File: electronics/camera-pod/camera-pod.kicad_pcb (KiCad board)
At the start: 2 copper layers, 40 x 27 mm, 16 parts, among them J1 LEAD, J2 MEGA, U1 AMS1117-3.3

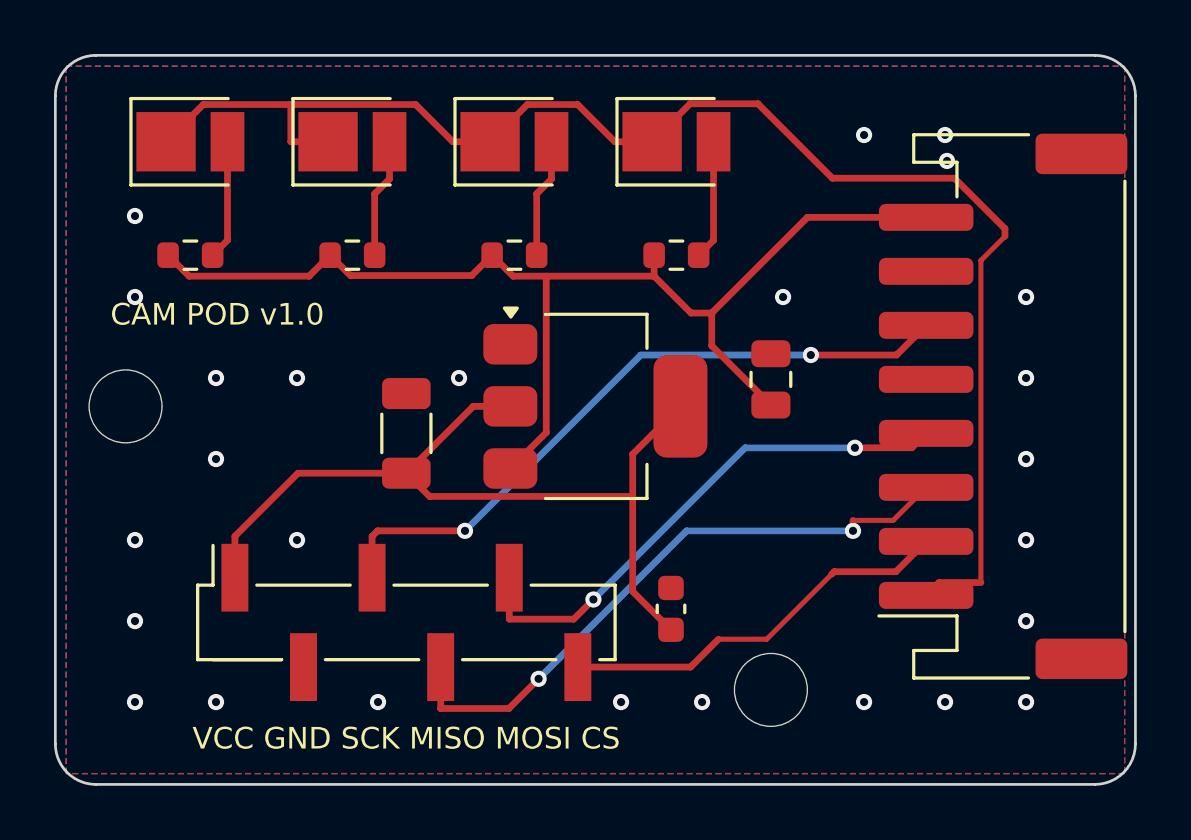
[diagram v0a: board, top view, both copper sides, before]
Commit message: Camera pod: the PCBA review's fixes
P1: the LED resistors are 100 Ohm 0805 (C17408, a basic part; no 82 Ohm
exists as a basic 0805 or 1206).  Over the LEDs' Vf spread at that
current (about 2.65-3.2 V) and CAM_5V at 5.0-5.2 V that gives 18-26 mA
per LED, at most 66 mW in a 125 mW resistor and 102 mA for the four,
inside the node's camera budget.  56 Ohm 0603 gave 36-44 mA and up to
108 mW in 100 mW.  The light drops by about a third from the 32 mA
first planned, about 0.6 EV, which the Mega's auto-exposure takes.
P2: the AMS1117's ringing on its 22 uF MLCC is on the bring-up list,
with the LED current.  P3: a CAM_5V load switch on IO5/IO6 noted for a
later node.

The CPL audit agrees on all 14 parts.  ERC 0, DRC 0, parity 0, 0
unconnected; the BOM follows.

Co-Authored-By: Claude Opus 5.5 <noreply@anthropic.com>
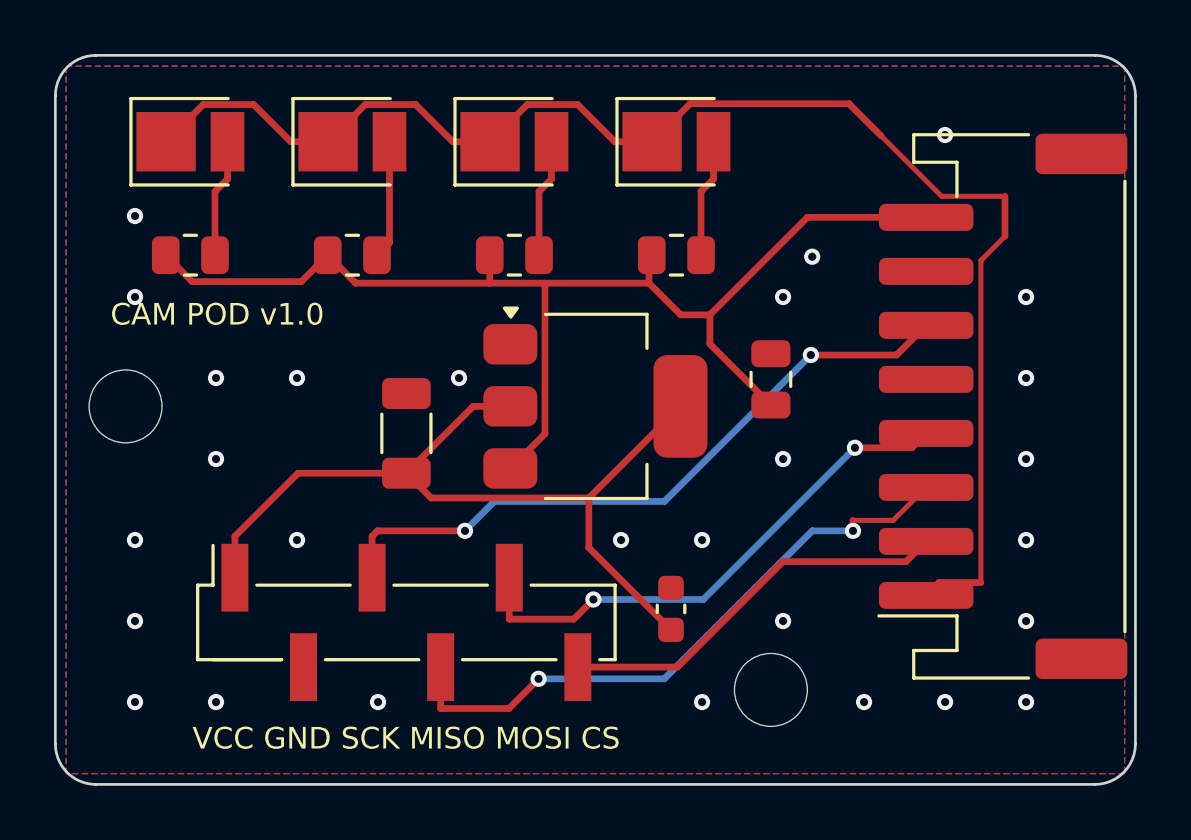
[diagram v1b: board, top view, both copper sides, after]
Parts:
- R1, R2, R3, R4: value 56 -> 100; footprint Resistor_SMD:R_0603_1608Metric -> Resistor_SMD:R_0805_2012Metric
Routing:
- net /Pod/LED_K: track 54.3 -> 53.4 mm
- net /Pod/CAM_5V: track 44.5 -> 45.2 mm
- net GND: vias 26 -> 28

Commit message: Power pads connect solid on the DATA ×4, the DATA port and the camera pod
The rule from d58f976, applied to the three boards. Each one declares its power nets in design.py:
- DATA ×4: GND, +5V, each port's 5V_SW and VBUS
- DATA port: GND, VBUS
- camera pod: GND, CAM_5V
pcbgen then connects their IC and connector pins solid to the pours. A small part with an end on a
track keeps its reliefs. The .kicad_dru carries both rules.

Now solid:
- DATA ×4: the four receptacles' and J1's GND pins; the hub's, expanders', INA226s', switches' and
  ESDs' GND pins and exposed pads; the LDO's VIN, EN and GND on its islands. Eighteen GND pads the
  pour didn't reach (USB4105 A1/A12/B1/B12 among them) now take it directly, and their tie tracks go
  (25 segments, 11 vias). The ports' 5V_SW and VBUS run in tracks, so their pads don't change.
- DATA port: J1's four GND pins, J2's two, the ESD's GND.
- Camera pod: J1's two GND pins, J2's GND, the AMS1117's GND.

Worst relieved power-net pad, before → after:
- DATA ×4: INA226 GND (U102.7) on 1 spoke, 0.29 mm → solid. Now the worst is a GND decoupling cap or
  pull-down (C201.2, R201.2...) on 1 spoke of 0.40 mm, a signal-level current.
- DATA port: J1's GND pins and U1.2 on 1 spoke, 0.40 mm → solid. Now the worst is C1 / C2 / the shell
  tabs on 3 spokes, 1.20 mm.
- Camera pod: U1.1, J1.5 / J1.7, C1, C3 on 3 spokes, 1.20 mm. Now U1.1 and J1's GND are solid; the
  worst is C1 / C3 on 3 spokes, 1.20 mm.

Same routes re-imported: only GND ties and stitching vias move. ERC/DRC 0, parity 0, 0 unconnected on
all three. CPL and BOM unchanged, so the CPL audit stands. Renders, PDFs and gerbers regenerated.

Co-Authored-By: Claude Opus 5.5 <noreply@anthropic.com>
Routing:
- net GND: vias 28 -> 32

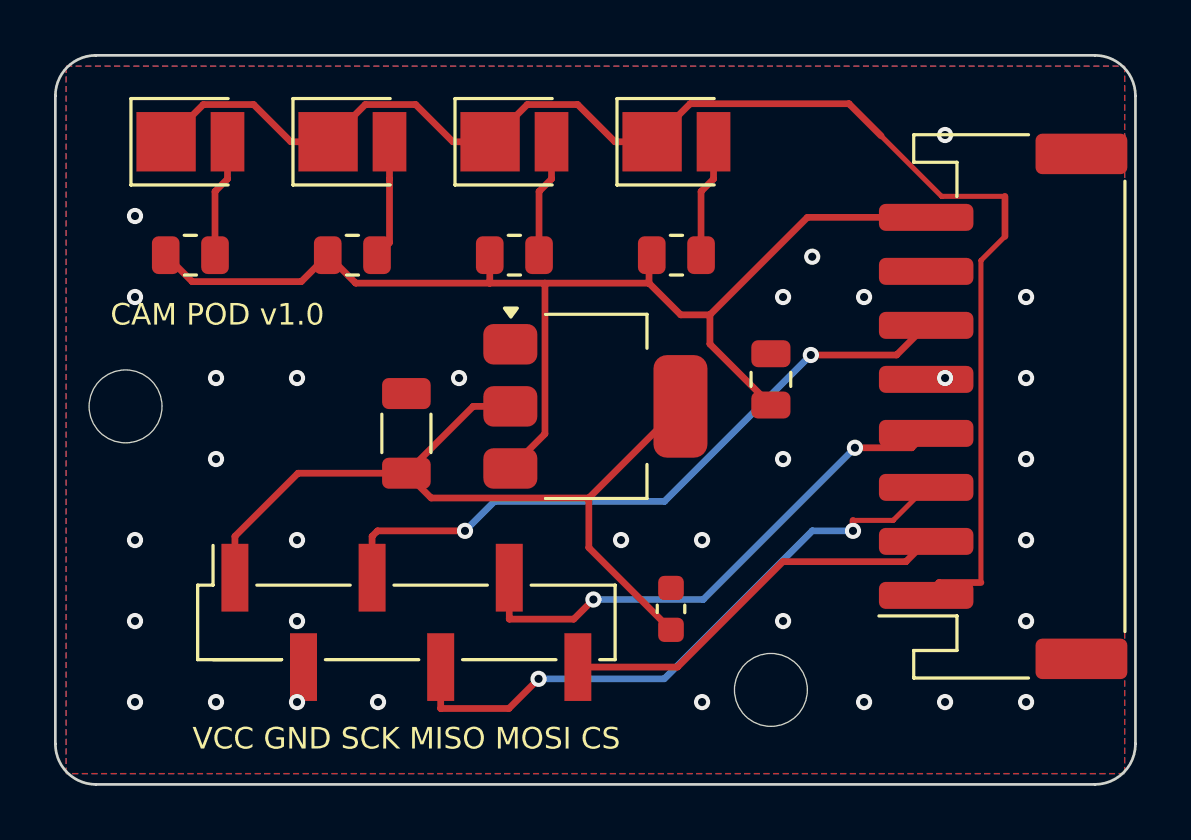
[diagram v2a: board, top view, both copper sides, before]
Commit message: Boards: tracks straightened after routing, bends ranked; bay node and hub re-routed
Freerouting leaves staircases of 45° and straight segments where one bend
would do: they are no longer than the straight route, so nothing preferred it.

- pcbgen.tidy_tracks now runs on every board after the import: a run of up
  to 12 router segments becomes the fewest straight and 45° segments joining
  its ends (octilinear.py: one, one bend, or a dogleg on one of the run's own
  lines), at no more length and with every clearance kept.  Differential
  pairs, drawn tracks, exclusive cores, fan-out reservations and footprint
  keep-outs are left alone.  tools/kicad.sh <board> --tidy runs it on a
  routed board without re-routing.
- route_metrics counts bends; route_farm ranks them at 0.5 mm each.
- Bay node: In2's +5V outline stops at x 21.7, off the +3V3 one.  Re-routed
  by the portfolio (noneck): 504 bends, 435 vias, 2183 mm (was 631, 401, 2270).
- Power hub: buck-vin is exclusive (14 of 17 runs clean, 2 before).
  Re-routed (planevia50): 655 bends, 436 vias, 3447 mm (was 767, 433, 3537).
- DATA x4 v2: the drawn switch feeds stay (no clean run without them); its
  routing straightened in place, the tidy settings now the default.
- Camera pod straightened in place (59 -> 48 bends); data port unchanged.

ERC, copper DRC and parity clean on all five; fab outputs, the DATA x4 v2
panel and the viewer's models regenerated.

Co-Authored-By: Claude Opus 5.5 <noreply@anthropic.com>
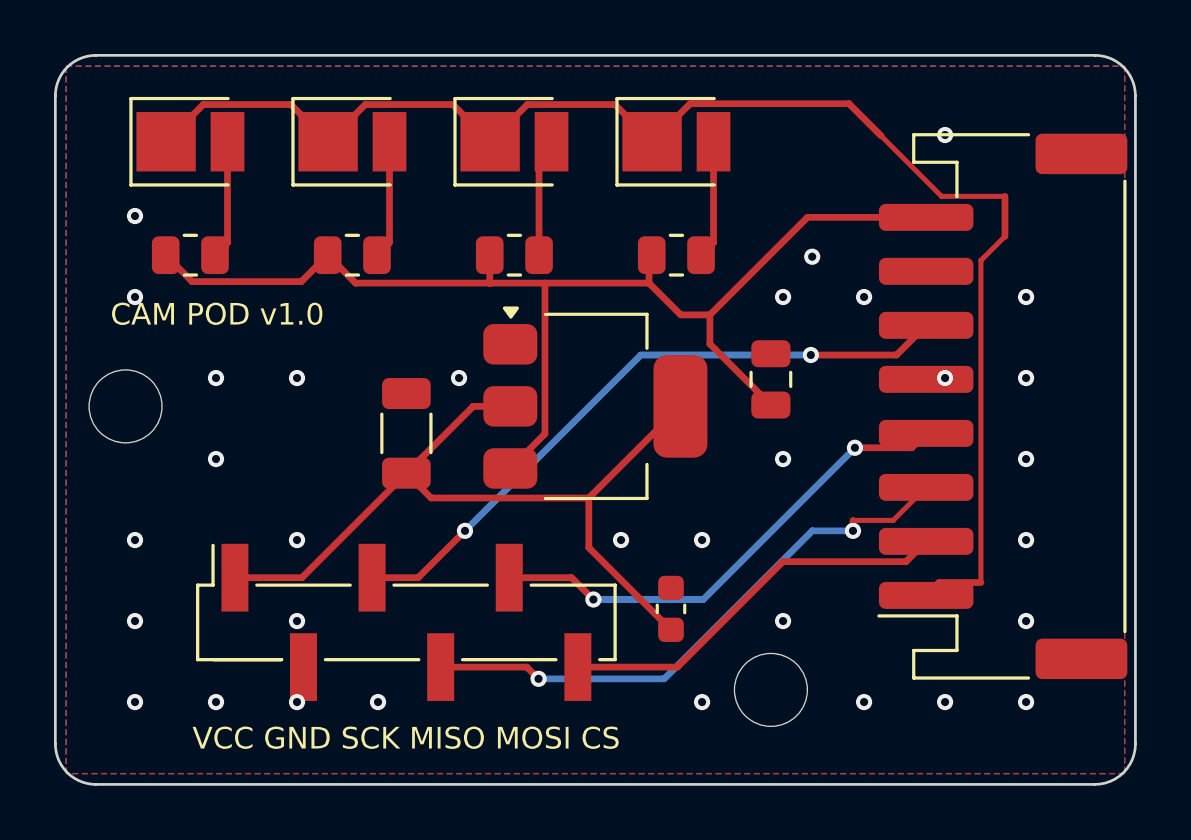
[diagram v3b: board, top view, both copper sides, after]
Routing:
- net /Pod/MISO: track 23.1 -> 21.3 mm
- net /Pod/MOSI: track 19.8 -> 18.3 mm
- net /Pod/SCK: track 25.3 -> 24.4 mm
- net +3V3: track 31.8 -> 30.9 mm
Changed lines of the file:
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@@
-	)
-	(segment
-		(start 13 15.475)
-		(end 8.9863 15.475)
-		(width 0.25)
-		(layer "F.Cu")
-		(net "+3V3")
 	)
 	(segment
@@
 	)
 	(segment
+		(start 13 15.475)
+		(end 9.13 19.345)
+		(width 0.25)
+		(layer "F.Cu")
+		(net "+3V3")
+	)
+	(segment
 		(start 15.475 13)
 		(end 16.85 13)
@@
 	)
 	(segment
-		(start 8.9863 15.475)
-		(end 6.65 17.8113)
-		(width 0.25)
-		(layer "F.Cu")
-		(net "+3V3")
-	)
-	(segment
-		(start 6.65 19.345)
-		(end 6.65 17.8113)
+		(start 9.13 19.345)
+		(end 6.65 19.345)
 		(width 0.25)
 		(layer "F.Cu")
@@
 	)
 	(segment
-		(start 11.9313 17.61)
-		(end 11.73 17.8113)
+		(start 13.4355 19.345)
+		(end 11.73 19.345)
 		(width 0.25)
 		(layer "F.Cu")
@@
 	(segment
 		(start 15.1705 17.61)
-		(end 11.9313 17.61)
+		(end 13.4355 19.345)
 		(width 0.25)
 		(layer "F.Cu")
 		(net "/Pod/SCK")
 	)
-	(segment
-		(start 11.73 19.345)
-		(end 11.73 17.8113)
-		(width 0.25)
-		(layer "F.Cu")
+	(via
+		(at 27.9793 11.0976)
+		(size 0.6)
+		(drill 0.3)
+		(layers "F.Cu" "B.Cu")
 		(net "/Pod/SCK")
 	)
 	(via
-		(at 27.9793 11.0976)
+		(at 15.1705 17.61)
 		(size 0.6)
 		(drill 0.3)
@@
 		(net "/Pod/SCK")
 	)
-	(via
-		(at 15.1705 17.61)
-		(size 0.6)
-		(drill 0.3)
-		(layers "F.Cu" "B.Cu")
-		(net "/Pod/SCK")
-	)
-	(segment
-		(start 22.5581 16.5188)
-		(end 16.2617 16.5188)
+	(segment
+		(start 21.6829 11.0976)
+		(end 15.1705 17.61)
 		(width 0.25)
 		(layer "B.Cu")
@@
 	(segment
 		(start 27.9793 11.0976)
-		(end 22.5581 16.5188)
+		(end 21.6829 11.0976)
 		(width 0.25)
 		(layer "B.Cu")
 		(net "/Pod/SCK")
-	)
-	(segment
-		(start 16.2617 16.5188)
-		(end 15.1705 17.61)
-		(width 0.25)
-		(layer "B.Cu")
-		(net "/Pod/SCK")
-	)
-	(segment
-		(start 17.8955 23.09)
-		(end 16.7968 24.1887)
-		(width 0.25)
-		(layer "F.Cu")
-		(net "/Pod/MISO")
 	)
 	(segment
@@
 	)
 	(segment
+		(start 17.8955 23.09)
+		(end 17.4605 22.655)
+		(width 0.25)
+		(layer "F.Cu")
+		(net "/Pod/MISO")
+	)
+	(segment
+		(start 17.4605 22.655)
+		(end 14.27 22.655)
+		(width 0.25)
+		(layer "F.Cu")
+		(net "/Pod/MISO")
+	)
+	(segment
 		(start 29.5398 17.61)
 		(end 29.5398 17.2218)
@@
 		(net "/Pod/MISO")
 	)
-	(segment
-		(start 14.27 22.655)
-		(end 14.27 24.1887)
-		(width 0.25)
-		(layer "F.Cu")
-		(net "/Pod/MISO")
-	)
-	(segment
-		(start 16.7968 24.1887)
-		(end 14.27 24.1887)
-		(width 0.25)
-		(layer "F.Cu")
-		(net "/Pod/MISO")
-	)
 	(via
 		(at 29.5398 17.61)
@@
 	)
 	(segment
-		(start 19.9264 20.152)
-		(end 19.1997 20.8787)
+		(start 19.1194 19.345)
+		(end 16.81 19.345)
 		(width 0.25)
 		(layer "F.Cu")
@@
 	)
 	(segment
+		(start 19.9264 20.152)
+		(end 19.1194 19.345)
+		(width 0.25)
+		(layer "F.Cu")
+		(net "/Pod/MOSI")
+	)
+	(segment
 		(start 31.7167 14.5333)
 		(end 32.25 14)
@@
 		(net "/Pod/MOSI")
 	)
-	(segment
-		(start 19.1997 20.8787)
-		(end 16.81 20.8787)
-		(width 0.25)
-		(layer "F.Cu")
-		(net "/Pod/MOSI")
-	)
-	(segment
-		(start 16.81 19.345)
-		(end 16.81 20.8787)
-		(width 0.25)
-		(layer "F.Cu")
-		(net "/Pod/MOSI")
-	)
 	(via
 		(at 29.6116 14.5333)
@@
 	)
 	(segment
-		(start 5.9125 5.0412)
-		(end 5.9125 7.4)
+		(start 5.9125 7.4)
+		(end 6.375 6.9375)
 		(width 0.25)
 		(layer "F.Cu")
@@
 	)
 	(segment
-		(start 6.375 3.2)
-		(end 6.375 4.5787)
+		(start 6.375 6.9375)
+		(end 6.375 3.2)
 		(width 0.25)
 		(layer "F.Cu")
 		(net "/Pod/LED_A1")
-	)
-	(segment
-		(start 6.375 4.5787)
-		(end 5.9125 5.0412)
-		(width 0.25)
-		(layer "F.Cu")
-		(net "/Pod/LED_A1")
-	)
-	(segment
-		(start 10.1 3.2)
-		(end 11.4787 1.8213)
-		(width 0.25)
-		(layer "F.Cu")
-		(net "/Pod/LED_K")
 	)
 	(segment
@@
 	)
 	(segment
-		(start 19.3426 1.8213)
-		(end 20.7213 3.2)
+		(start 11.4787 1.8213)
+		(end 14.7213 1.8213)
 		(width 0.25)
 		(layer "F.Cu")
@@
 		(start 16.1 3.2)
 		(end 17.4787 1.8213)
+		(width 0.25)
+		(layer "F.Cu")
+		(net "/Pod/LED_K")
+	)
+	(segment
+		(start 8.7213 1.8213)
+		(end 5.4787 1.8213)
 		(width 0.25)
 		(layer "F.Cu")
@@
 	)
 	(segment
-		(start 13.3426 1.8213)
-		(end 14.7213 3.2)
+		(start 35.1678 6.7055)
+		(end 35.1678 5.2218)
+		(width 0.25)
+		(layer "F.Cu")
+		(net "/Pod/LED_K")
+	)
+	(segment
+		(start 32.7257 19.5243)
+		(end 34.2781 19.5243)
+		(width 0.25)
+		(layer "F.Cu")
+		(net "/Pod/LED_K")
+	)
+	(segment
+		(start 10.1 3.2)
+		(end 11.4787 1.8213)
+		(width 0.25)
+		(layer "F.Cu")
+		(net "/Pod/LED_K")
+	)
+	(segment
+		(start 14.7213 1.8213)
+		(end 16.1 3.2)
+		(width 0.25)
+		(layer "F.Cu")
+		(net "/Pod/LED_K")
+	)
+	(segment
+		(start 29.3919 1.7918)
+		(end 23.5082 1.7918)
+		(width 0.25)
+		(layer "F.Cu")
+		(net "/Pod/LED_K")
+	)
+	(segment
+		(start 20.7213 1.8213)
+		(end 22.1 3.2)
+		(width 0.25)
+		(layer "F.Cu")
+		(net "/Pod/LED_K")
+	)
+	(segment
+		(start 32.25 20)
+		(end 32.7257 19.5243)
 		(width 0.25)
 		(layer "F.Cu")
@@
 	)
 	(segment
-		(start 35.1678 6.7055)
-		(end 35.1678 5.2218)
-		(width 0.25)
-		(layer "F.Cu")
-		(net "/Pod/LED_K")
-	)
-	(segment
-		(start 32.7257 19.5243)
-		(end 34.2781 19.5243)
-		(width 0.25)
-		(layer "F.Cu")
-		(net "/Pod/LED_K")
-	)
-	(segment
-		(start 8.7213 3.2)
-		(end 7.3426 1.8213)
-		(width 0.25)
-		(layer "F.Cu")
-		(net "/Pod/LED_K")
-	)
-	(segment
-		(start 29.3919 1.7918)
-		(end 23.5082 1.7918)
-		(width 0.25)
-		(layer "F.Cu")
-		(net "/Pod/LED_K")
-	)
-	(segment
-		(start 16.1 3.2)
-		(end 14.7213 3.2)
-		(width 0.25)
-		(layer "F.Cu")
-		(net "/Pod/LED_K")
-	)
-	(segment
-		(start 7.3426 1.8213)
-		(end 5.4787 1.8213)
-		(width 0.25)
-		(layer "F.Cu")
-		(net "/Pod/LED_K")
-	)
-	(segment
-		(start 32.25 20)
-		(end 32.7257 19.5243)
-		(width 0.25)
-		(layer "F.Cu")
-		(net "/Pod/LED_K")
-	)
-	(segment
-		(start 10.1 3.2)
-		(end 8.7213 3.2)
-		(width 0.25)
-		(layer "F.Cu")
-		(net "/Pod/LED_K")
-	)
-	(segment
-		(start 17.4787 1.8213)
-		(end 19.3426 1.8213)
-		(width 0.25)
-		(layer "F.Cu")
-		(net "/Pod/LED_K")
-	)
-	(segment
-		(start 11.4787 1.8213)
-		(end 13.3426 1.8213)
-		(width 0.25)
-		(layer "F.Cu")
-		(net "/Pod/LED_K")
-	)
-	(segment
-		(start 22.1 3.2)
-		(end 20.7213 3.2)
-		(width 0.25)
-		(layer "F.Cu")
-		(net "/Pod/LED_K")
-	)
-	(segment
 		(start 30.5837 2.9836)
 		(end 29.3919 1.7918)
+		(width 0.25)
+		(layer "F.Cu")
+		(net "/Pod/LED_K")
+	)
+	(segment
+		(start 17.4787 1.8213)
+		(end 20.7213 1.8213)
 		(width 0.25)
 		(layer "F.Cu")
@@
 	)
 	(segment
+		(start 10.1 3.2)
+		(end 8.7213 1.8213)
+		(width 0.25)
+		(layer "F.Cu")
+		(net "/Pod/LED_K")
+	)
+	(segment
 		(start 23.5082 1.7918)
 		(end 22.1 3.2)
@@
 	(segment
 		(start 12.375 6.9375)
-		(end 11.9125 7.4)
+		(end 12.375 3.2)
 		(width 0.25)
 		(layer "F.Cu")
@@
 	)
 	(segment
-		(start 12.375 4.5787)
+		(start 11.9125 7.4)
 		(end 12.375 6.9375)
 		(width 0.25)
@@
 	)
 	(segment
-		(start 12.375 3.2)
-		(end 12.375 4.5787)
-		(width 0.25)
-		(layer "F.Cu")
-		(net "/Pod/LED_A2")
-	)
-	(segment
-		(start 23.9125 5.0412)
-		(end 24.375 4.5787)
+		(start 23.9125 7.4)
+		(end 24.375 6.9375)
 		(width 0.25)
 		(layer "F.Cu")
@@
 	)
 	(segment
-		(start 23.9125 7.4)
-		(end 23.9125 5.0412)
+		(start 24.375 6.9375)
+		(end 24.375 3.2)
 		(width 0.25)
 		(layer "F.Cu")
@@
 	)
 	(segment
-		(start 24.375 3.2)
-		(end 24.375 4.5787)
-		(width 0.25)
-		(layer "F.Cu")
-		(net "/Pod/LED_A4")
-	)
-	(segment
 		(start 18.375 3.2)
-		(end 18.375 4.5787)
+		(end 17.9125 3.6625)
 		(width 0.25)
 		(layer "F.Cu")
@@
 	)
 	(segment
-		(start 17.9125 5.0412)
-		(end 18.375 4.5787)
-		(width 0.25)
-		(layer "F.Cu")
-		(net "/Pod/LED_A3")
-	)
-	(segment
-		(start 17.9125 7.4)
-		(end 17.9125 5.0412)
-		(width 0.25)
-		(layer "F.Cu")
+		(start 17.9125 3.6625)
+		(end 17.9125 7.4)
+		(width 0.25)
+		(layer "F.Cu")
